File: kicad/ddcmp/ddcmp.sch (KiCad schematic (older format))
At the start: 0 parts

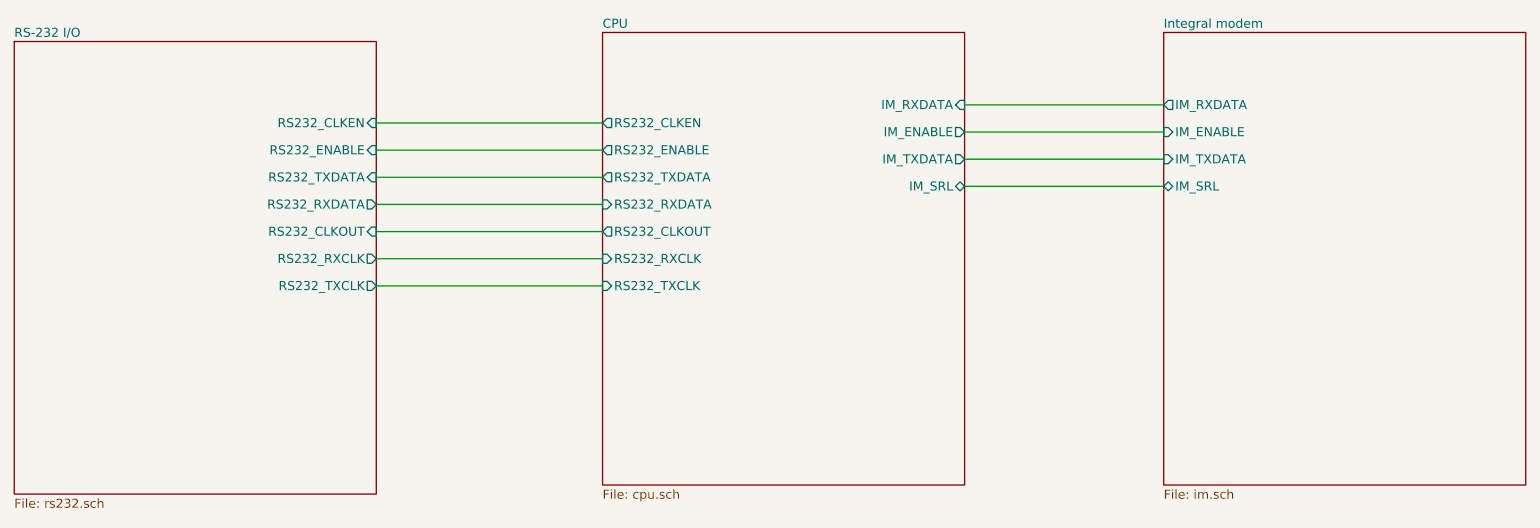
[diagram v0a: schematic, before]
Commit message: Finish the connector hookups, to be verified carefully against DMR-11 schematics.
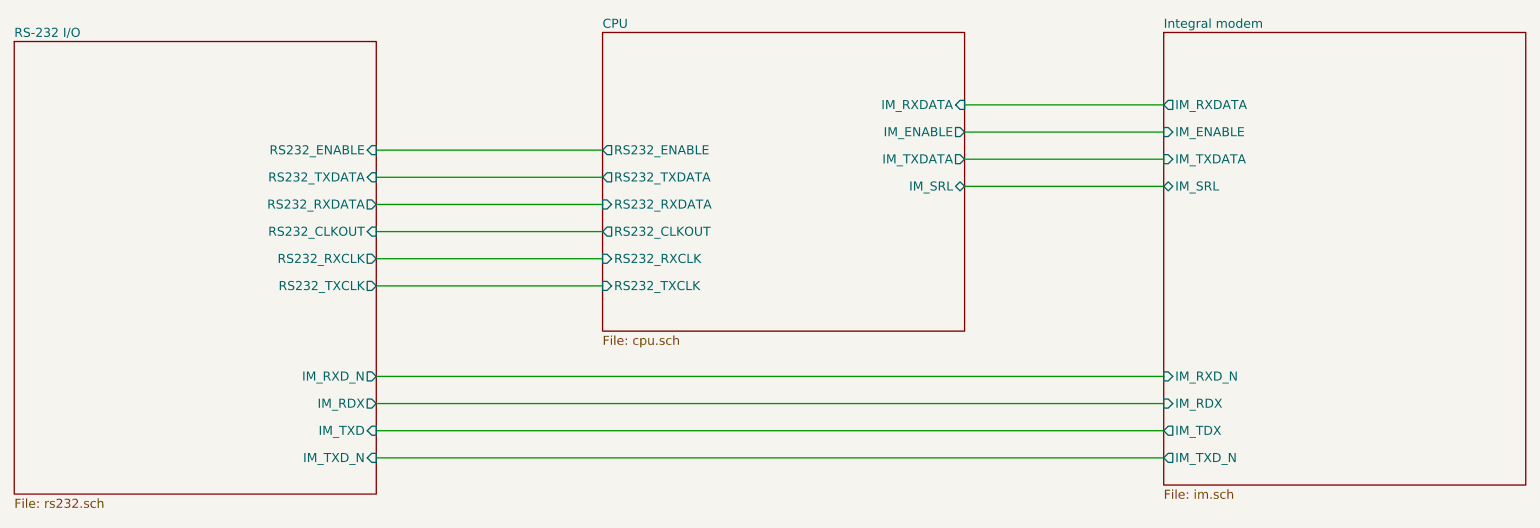
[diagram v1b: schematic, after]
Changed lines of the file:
@@
 $EndDescr
 $Sheet
-S 4850 2600 2000 2500
+S 4850 2600 2000 1650
 U 60A46E24
 F0 "CPU" 50
@@
 F4 "IM_TXDATA" O R 6850 3300 50
 F5 "IM_RXDATA" I R 6850 3000 50
-F6 "RS232_CLKEN" O L 4850 3100 50
-F7 "RS232_ENABLE" O L 4850 3250 50
-F8 "RS232_CLKOUT" O L 4850 3700 50
-F9 "RS232_TXCLK" I L 4850 4000 50
-F10 "RS232_RXDATA" I L 4850 3550 50
-F11 "RS232_RXCLK" I L 4850 3850 50
-F12 "RS232_TXDATA" O L 4850 3400 50
+F6 "RS232_ENABLE" O L 4850 3250 50
+F7 "RS232_CLKOUT" O L 4850 3700 50
+F8 "RS232_TXCLK" I L 4850 4000 50
+F9 "RS232_RXDATA" I L 4850 3550 50
+F10 "RS232_RXCLK" I L 4850 3850 50
+F11 "RS232_TXDATA" O L 4850 3400 50
 $EndSheet
 $Sheet
@@
 F4 "IM_TXDATA" I L 7950 3300 50
 F5 "IM_SRL" T L 7950 3450 50
+F6 "IM_TXD_N" O L 7950 4950 50
+F7 "IM_TDX" O L 7950 4800 50
+F8 "IM_RXD_N" I L 7950 4500 50
+F9 "IM_RDX" I L 7950 4650 50
 $EndSheet
 $Sheet
@@
 F0 "RS-232 I/O" 50
 F1 "rs232.sch" 50
-F2 "RS232_CLKEN" I R 3600 3100 50
-F3 "RS232_ENABLE" I R 3600 3250 50
-F4 "RS232_TXDATA" I R 3600 3400 50
-F5 "RS232_RXDATA" O R 3600 3550 50
-F6 "RS232_CLKOUT" I R 3600 3700 50
-F7 "RS232_RXCLK" O R 3600 3850 50
-F8 "RS232_TXCLK" O R 3600 4000 50
+F2 "RS232_ENABLE" I R 3600 3250 50
+F3 "RS232_TXDATA" I R 3600 3400 50
+F4 "RS232_RXDATA" O R 3600 3550 50
+F5 "RS232_CLKOUT" I R 3600 3700 50
+F6 "RS232_RXCLK" O R 3600 3850 50
+F7 "RS232_TXCLK" O R 3600 4000 50
+F8 "IM_RXD_N" O R 3600 4500 50
+F9 "IM_RDX" O R 3600 4650 50
+F10 "IM_TXD" I R 3600 4800 50
+F11 "IM_TXD_N" I R 3600 4950 50
 $EndSheet
-Wire Wire Line
-	4850 3100 3600 3100
 Wire Wire Line
 	3600 3250 4850 3250
@@
 Wire Wire Line
 	7950 3450 6850 3450
+Wire Wire Line
+	3600 4950 7950 4950
+Wire Wire Line
+	3600 4500 7950 4500
+Wire Wire Line
+	3600 4650 7950 4650
+Wire Wire Line
+	7950 4800 3600 4800
 $EndSCHEMATC

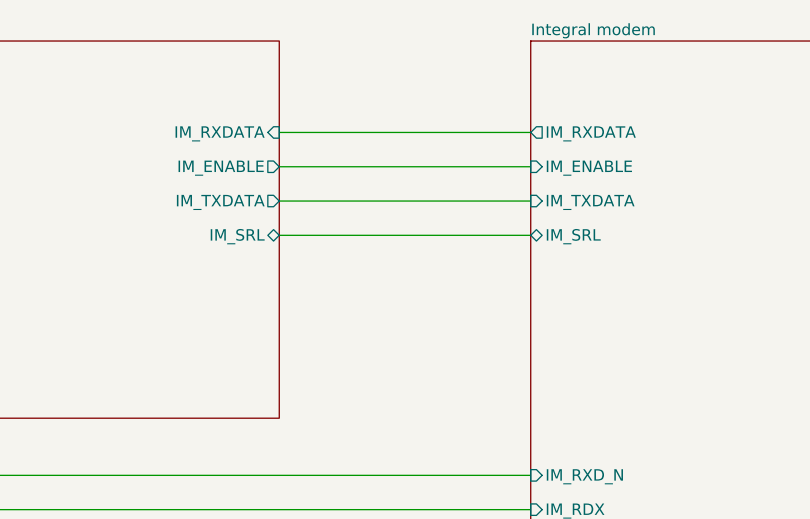
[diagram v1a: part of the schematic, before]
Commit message: Complete schematic, PCB layout, and matching code.  Needs testing.
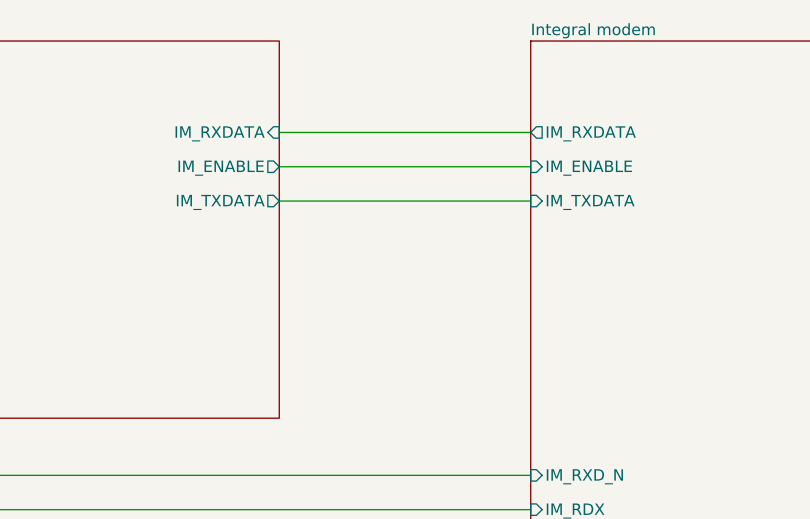
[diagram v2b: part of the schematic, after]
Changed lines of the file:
@@
 Rev "A"
 Comp "AK Design"
-Comment1 ""
+Comment1 "Copyright © 2021 by Paul Koning, NI1D"
 Comment2 ""
 Comment3 ""
 Comment4 ""
 $EndDescr
-$Sheet
-S 4850 2600 2000 1650
-U 60A46E24
-F0 "CPU" 50
-F1 "cpu.sch" 50
-F2 "IM_SRL" T R 6850 3450 50
-F3 "IM_ENABLE" O R 6850 3150 50
-F4 "IM_TXDATA" O R 6850 3300 50
-F5 "IM_RXDATA" I R 6850 3000 50
-F6 "RS232_ENABLE" O L 4850 3250 50
-F7 "RS232_CLKOUT" O L 4850 3700 50
-F8 "RS232_TXCLK" I L 4850 4000 50
-F9 "RS232_RXDATA" I L 4850 3550 50
-F10 "RS232_RXCLK" I L 4850 3850 50
-F11 "RS232_TXDATA" O L 4850 3400 50
-$EndSheet
 $Sheet
 S 7950 2600 2000 2500
@@
 F3 "IM_ENABLE" I L 7950 3150 50
 F4 "IM_TXDATA" I L 7950 3300 50
-F5 "IM_SRL" T L 7950 3450 50
-F6 "IM_TXD_N" O L 7950 4950 50
-F7 "IM_TDX" O L 7950 4800 50
-F8 "IM_RXD_N" I L 7950 4500 50
-F9 "IM_RDX" I L 7950 4650 50
+F5 "IM_TXD_N" O L 7950 4950 50
+F6 "IM_TDX" O L 7950 4800 50
+F7 "IM_RXD_N" I L 7950 4500 50
+F8 "IM_RDX" I L 7950 4650 50
 $EndSheet
 $Sheet
@@
 	6850 3300 7950 3300
 Wire Wire Line
-	7950 3450 6850 3450
-Wire Wire Line
 	3600 4950 7950 4950
 Wire Wire Line
@@
 Wire Wire Line
 	7950 4800 3600 4800
+$Sheet
+S 4850 2600 2000 1650
+U 60A46E24
+F0 "CPU" 50
+F1 "cpu.sch" 50
+F2 "IM_ENABLE" O R 6850 3150 50
+F3 "IM_TXDATA" O R 6850 3300 50
+F4 "IM_RXDATA" I R 6850 3000 50
+F5 "RS232_ENABLE" O L 4850 3250 50
+F6 "RS232_CLKOUT" O L 4850 3700 50
+F7 "RS232_TXCLK" I L 4850 4000 50
+F8 "RS232_RXDATA" I L 4850 3550 50
+F9 "RS232_RXCLK" I L 4850 3850 50
+F10 "RS232_TXDATA" O L 4850 3400 50
+$EndSheet
 $EndSCHEMATC

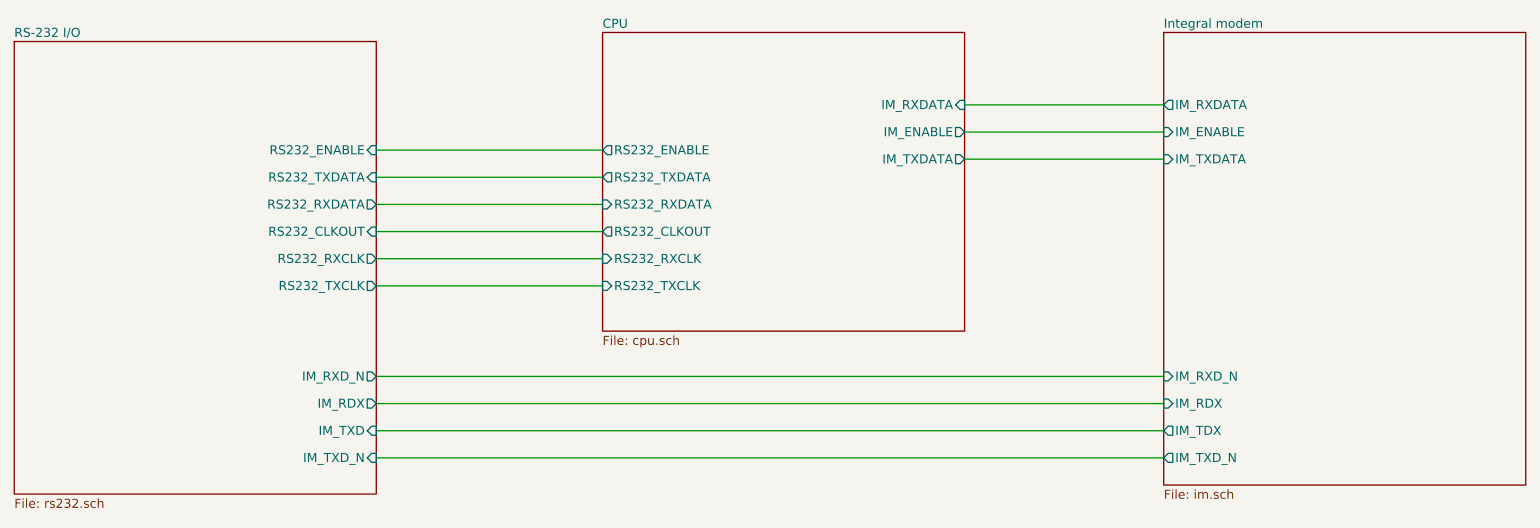
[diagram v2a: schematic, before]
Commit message: Documentation improvements, small schematic fixes. Also firmware improvements, particularly clock rate accuracy.
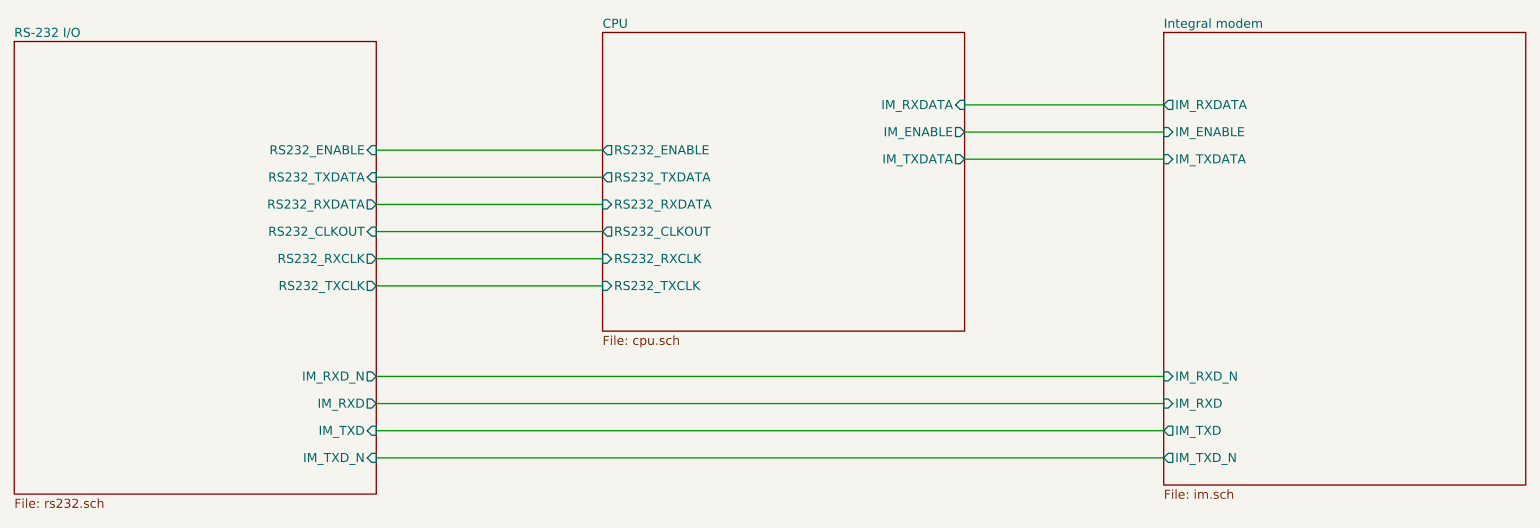
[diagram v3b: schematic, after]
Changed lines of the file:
@@
 F4 "IM_TXDATA" I L 7950 3300 50
 F5 "IM_TXD_N" O L 7950 4950 50
-F6 "IM_TDX" O L 7950 4800 50
+F6 "IM_TXD" O L 7950 4800 50
 F7 "IM_RXD_N" I L 7950 4500 50
-F8 "IM_RDX" I L 7950 4650 50
+F8 "IM_RXD" I L 7950 4650 50
 $EndSheet
 $Sheet
@@
 F7 "RS232_TXCLK" O R 3600 4000 50
 F8 "IM_RXD_N" O R 3600 4500 50
-F9 "IM_RDX" O R 3600 4650 50
+F9 "IM_RXD" O R 3600 4650 50
 F10 "IM_TXD" I R 3600 4800 50
 F11 "IM_TXD_N" I R 3600 4950 50
